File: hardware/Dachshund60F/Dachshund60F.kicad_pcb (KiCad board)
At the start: 2 copper layers, 318.5 x 121.1 mm, 218 parts, among them J1 USB daughterboard (JST-SH 4P), J2 Battery (JST-PH 2P), J3 SWD, J4 Display, Q1 AO3401A, SW1 Power, SW100 MX Esc (1.00u), SW101 MX F1 (1.00u), SW102 MX F2 (1.00u), SW103 MX F3 (1.00u), SW104 MX F4 (1.00u), SW105 MX F5 (1.00u), SW106 MX F6 (1.00u), SW107 MX F7 (1.00u), SW108 MX F8 (1.00u), SW109 MX F9 (1.00u), SW110 MX F10 (1.00u), SW111 MX F11 (1.00u), SW112 MX F12 (1.00u), SW113 MX Delete (1.00u), SW2 Reset, SW200 MX ` (1.00u), SW201 MX 1 (1.00u), SW202 MX 2 (1.00u), SW203 MX 3 (1.00u), SW204 MX 4 (1.00u), SW205 MX 5 (1.00u), SW206 MX 6 (1.00u), SW207 MX 7 (1.00u), SW208 MX 8 (1.00u), SW209 MX 9 (1.00u), SW210 MX 0 (1.00u), SW211 MX - (1.00u), SW212 MX = (1.00u), SW213 MX Backspace (2.00u), SW3 PEC12R-4220F-S0024 (horizonta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, SW300 MX Tab (1.50u), SW301 MX Q (1.00u), SW302 MX W (1.00u), SW303 MX E (1.00u), SW304 MX R (1.00u), SW305 MX T (1.00u), SW306 MX Y (1.00u), SW307 MX U (1.00u), SW308 MX I (1.00u), SW309 MX O (1.00u), SW310 MX P (1.00u), SW311 MX [ (1.00u), SW312 MX ] (1.00u), SW313 MX \ (1.50u), SW400 MX Caps Lock (1.75u), SW401 MX A (1.00u), SW402 MX S (1.00u), SW403 MX D (1.00u), SW404 MX F (1.00u), SW405 MX G (1.00u), SW406 MX H (1.00u), SW407 MX J (1.00u), SW408 MX K (1.00u), SW409 MX L (1.00u), SW410 MX ; (1.00u), SW411 MX ' (1.00u), SW413 MX Enter (2.25u), SW500 MX Shift (2.25u), SW501 MX Z (1.00u), SW502 MX X (1.00u), SW503 MX C (1.00u), SW504 MX V (1.00u), SW505 MX B (1.00u), SW506 MX N (1.00u), SW507 MX M (1.00u), SW508 MX , (1.00u), SW509 MX . (1.00u), SW510 MX / (1.00u), SW512 MX Shift (1.75u), SW513 MX Up (1.00u), SW600 MX Ctrl (1.25u), SW601 MX Win (1.25u), SW603 MX Alt (1.25u), SW604 MX Mod (1.25u, solder)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

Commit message: Use the MDBT50Q-P1MV2 module on the keyboard and dongle
The -P1MV2 is the same Raytac nRF52840 module with a PCB trace antenna
instead of a chip antenna: same 15.5 x 10.5 mm body, same 61 pads,
antenna at the same end. Footprint and keep-outs are unchanged; only
the Value, MPN and LCSC (C5119772) fields and the docs change. It costs
about C$10.74 at JLC against C$25.71, for about 20 % less rated
open-air range.

Co-Authored-By: Claude Opus 5.5 <noreply@anthropic.com>
Claude-Session: https://claude.ai/code/session_01P5t8x38EvinT9rpFK5k2Rj
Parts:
- U1: value MDBT50Q-1MV2 -> MDBT50Q-P1MV2
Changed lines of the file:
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@@
 			)
 		)
-		(property "Value" "MDBT50Q-1MV2"
+		(property "Value" "MDBT50Q-P1MV2"
 			(at 0.2 -8.95 90)
 			(unlocked yes)

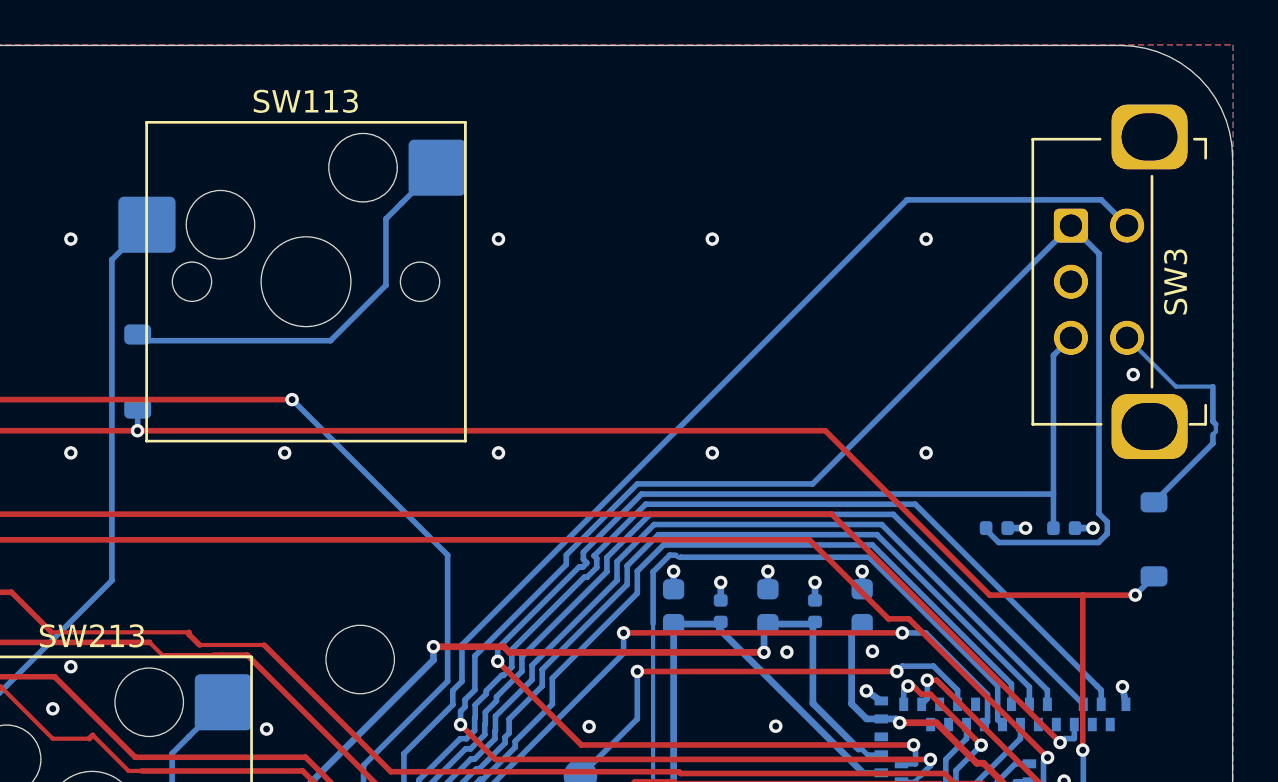
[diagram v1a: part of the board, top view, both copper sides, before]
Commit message: Mainboard: flip the roller encoder so its shaft points right
SW3 moves from (330.3, 47.025) at 0 deg to (314.3, 52.025) at 180 deg: the
body sits just right of the last key column and the shaft points toward the
board edge (tip at x ~331.3), so the wheel can be about 17 mm wide.

Reroute ENC_A, ENC_B, COL14 and ENC_SW to the new pads (one new ENC_A via),
dip ROW0 under the new lower mounting tab, drop the two GND stitching vias
the new pins landed on, move the back-side name/version/JLC text off the
pins and refill the zones. DRC is unchanged: 0 errors, 0 unconnected, 0
parity issues.

Regenerate the plate (the notch is unchanged) and refresh the STEP exports.
The case still has the old roller position; that's a scheduled task.

Co-Authored-By: Claude Opus 5.5 (1M context) <noreply@anthropic.com>
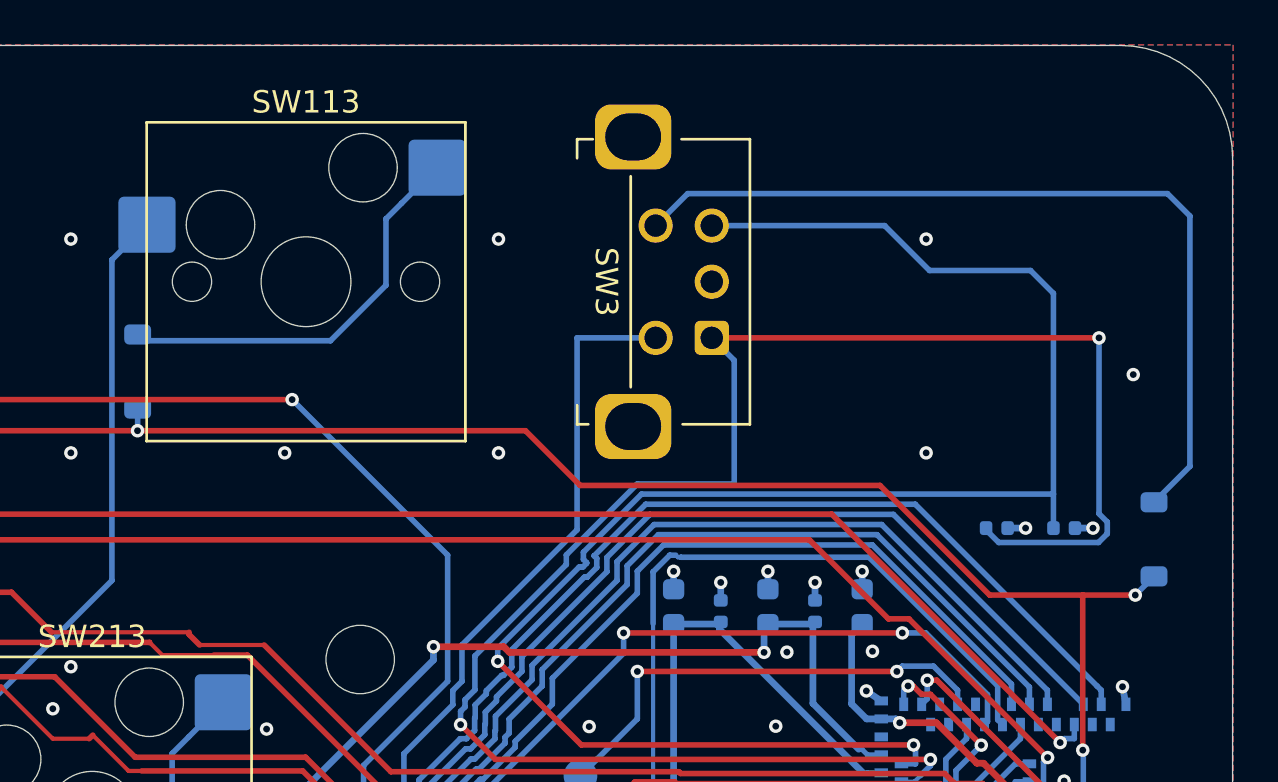
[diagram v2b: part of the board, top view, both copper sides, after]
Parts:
- moved SW3 16.8 mm to (314.3, 52.0), turned to 180 degrees
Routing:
- net /ENC_SW: track 11.1 -> 38.2 mm
- net /COL14: track 148.4 -> 129.4 mm
- net /ENC_B: track 59.0 -> 77.2 mm
- net /ENC_A: track 81.8 -> 80.7 mm, vias 2 -> 3
- net GND: vias 237 -> 235
